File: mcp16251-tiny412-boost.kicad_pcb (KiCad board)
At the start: 2 copper layers, 40.6 x 24.1 mm, 40 parts, among them J1 JST_PH_Header, J10 THT_Castellated, J11 THT_Castellated, J2 THT_Castellated, J3 THT_Castellated, J4 THT_Castellated, J5 THT_Castellated, J6 THT_Castellated, J7 THT_Castellated, J8 THT_Castellated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

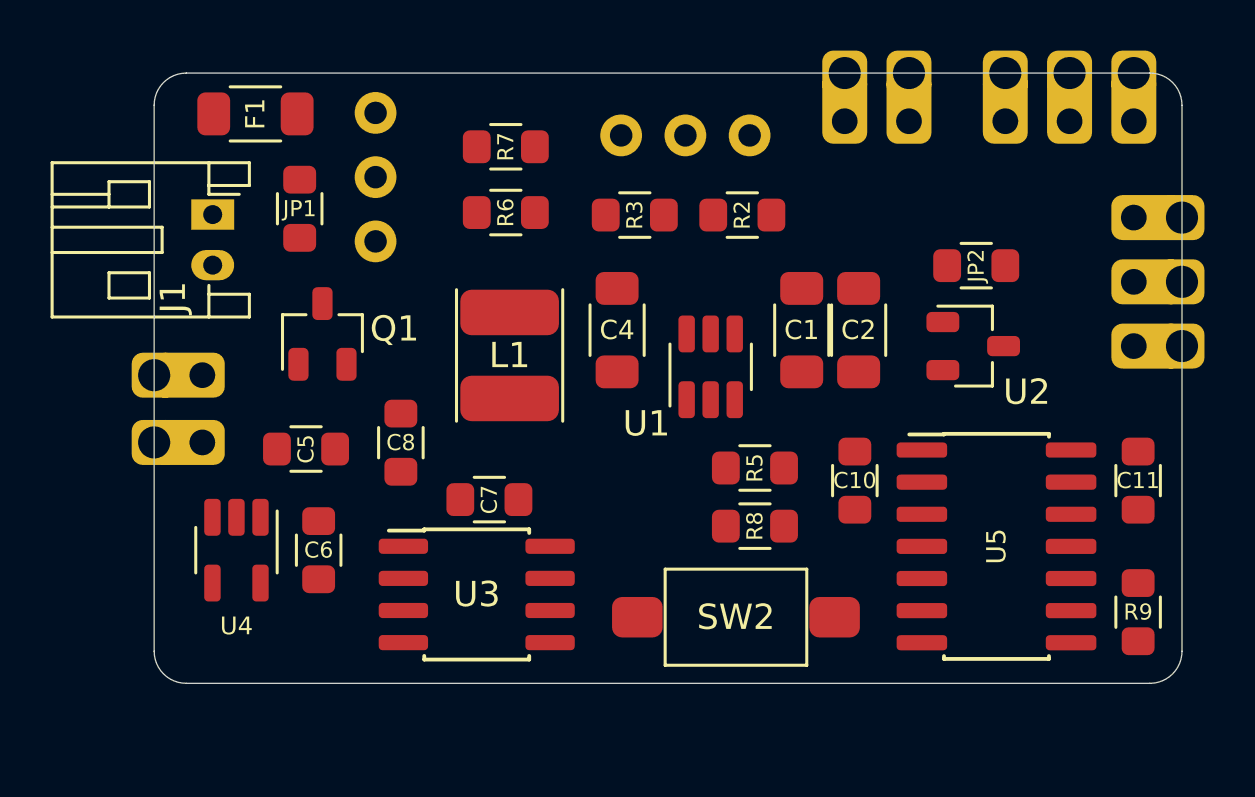
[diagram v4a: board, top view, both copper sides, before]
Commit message: Step-up converter sub-circuit wiring
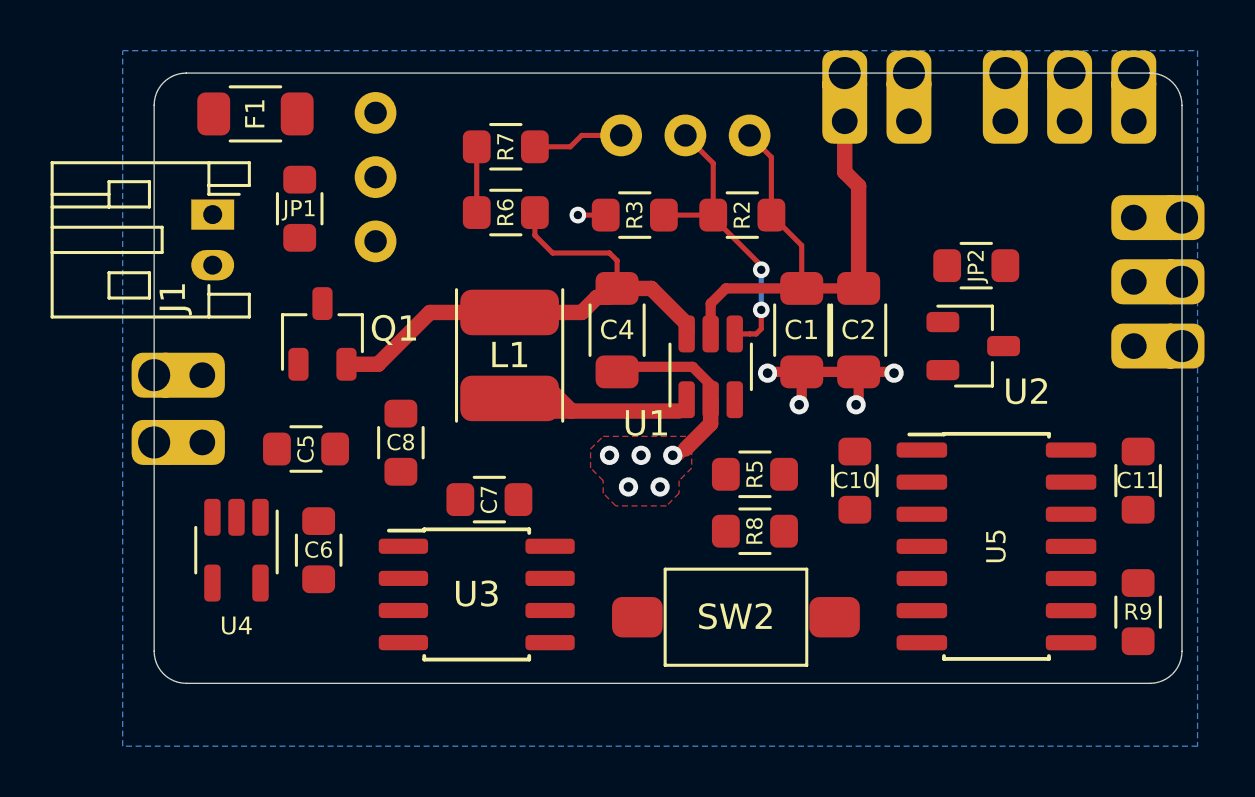
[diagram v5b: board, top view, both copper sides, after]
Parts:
- moved R5 0.25 mm to (142.5, 111.8)
- moved R8 0.20 mm to (142.5, 114.0)
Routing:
- net VBAT: track 0.00 -> 21.3 mm
- net 5V: track 0.00 -> 21.0 mm
- net GND: track 0.00 -> 20.1 mm, vias 0 -> 10
- net Net-(R2-Pad2): track 0.00 -> 12.0 mm, vias 0 -> 2
- net Net-(L1-Pad2): track 0.00 -> 6.56 mm
- net Net-(C8-Pad2): track 0.00 -> 2.60 mm
- added copper zone on B.Cu, net GND
- added copper zone on F.Cu, net GND
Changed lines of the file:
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@@
     (thickness 1.6)
     (drawings 12)
-    (tracks 0)
+    (tracks 74)
     (zones 0)
     (modules 40)
@@
   )
   (module MCP16251_module:0805_HS (layer F.Cu)
-    (at 142.5 111.5 180)
+    (at 142.5 111.75 180)
     (descr "Resistor SMD 0805, reflow soldering, Vishay (see dcrcw.pdf)")
     (tags "resistor 0805")
@@
   )
   (module MCP16251_module:0805_HS (layer F.Cu)
-    (at 142.5 113.8 180)
+    (at 142.5 114 180)
     (descr "Resistor SMD 0805, reflow soldering, Vishay (see dcrcw.pdf)")
     (tags "resistor 0805")
@@
     (arrow2b (pts (xy 118.745 129.54) (xy 119.871504 128.953579)))
   )
+  (via (at 138 111) (size 0.762) (drill 0.381) (layers F.Cu B.Cu) (net 1))
+  (segment (start 134.5 108.5) (end 135.25 109.25) (width 0.6096) (layer F.Cu) (net 4))
+  (segment (start 134 109.25) (end 139.5 109.25) (width 0.6096) (layer F.Cu) (net 4))
+  (segment (start 137.25 107.5) (end 137.05 107.7) (width 0.4064) (layer F.Cu) (net 1))
+  (segment (start 140.034562 107.5) (end 137.25 107.5) (width 0.4064) (layer F.Cu) (net 1))
+  (segment (start 140.75 108.215438) (end 140.034562 107.5) (width 0.4064) (layer F.Cu) (net 1))
+  (segment (start 140.75 108.8) (end 140.75 108.215438) (width 0.4064) (layer F.Cu) (net 1))
+  (segment (start 144.35 107.7) (end 146.6 107.7) (width 0.4064) (layer F.Cu) (net 1))
+  (via (at 139.25 111) (size 0.762) (drill 0.381) (layers F.Cu B.Cu) (net 1))
+  (segment (start 139.5 111) (end 139.25 111) (width 0.4064) (layer F.Cu) (net 1))
+  (via (at 136.75 111) (size 0.762) (drill 0.381) (layers F.Cu B.Cu) (net 1))
+  (via (at 138.75 112.25) (size 0.762) (drill 0.381) (layers F.Cu B.Cu) (net 1))
+  (via (at 137.5 112.25) (size 0.762) (drill 0.381) (layers F.Cu B.Cu) (net 1))
+  (segment (start 140.75 108.8) (end 140.75 109.75) (width 0.6096) (layer F.Cu) (net 1))
+  (segment (start 140.75 109.75) (end 139.75 110.75) (width 0.6096) (layer F.Cu) (net 1))
+  (segment (start 139.75 110.75) (end 139.5 111) (width 0.4064) (layer F.Cu) (net 1))
+  (segment (start 144.35 108.9) (end 144.25 109) (width 0.4064) (layer F.Cu) (net 1))
+  (via (at 144.25 109) (size 0.762) (drill 0.381) (layers F.Cu B.Cu) (net 1))
+  (segment (start 144.35 107.7) (end 144.35 108.9) (width 0.4064) (layer F.Cu) (net 1))
+  (via (at 146.5 109) (size 0.762) (drill 0.381) (layers F.Cu B.Cu) (net 1))
+  (segment (start 146.6 108.9) (end 146.5 109) (width 0.4064) (layer F.Cu) (net 1))
+  (segment (start 146.6 107.7) (end 146.6 108.9) (width 0.4064) (layer F.Cu) (net 1))
+  (via (at 148 107.75) (size 0.762) (drill 0.381) (layers F.Cu B.Cu) (net 1))
+  (segment (start 147.95 107.7) (end 148 107.75) (width 0.4064) (layer F.Cu) (net 1))
+  (segment (start 146.6 107.7) (end 147.95 107.7) (width 0.4064) (layer F.Cu) (net 1))
+  (via (at 143 107.75) (size 0.762) (drill 0.381) (layers F.Cu B.Cu) (net 1))
+  (segment (start 143.05 107.7) (end 143 107.75) (width 0.4064) (layer F.Cu) (net 1))
+  (segment (start 144.35 107.7) (end 143.05 107.7) (width 0.4064) (layer F.Cu) (net 1))
+  (segment (start 137.15 98.35) (end 137.21 98.35) (width 0.2032) (layer F.Cu) (net 1))
+  (segment (start 133.8 98.8) (end 135.2 98.8) (width 0.2032) (layer F.Cu) (net 1))
+  (segment (start 135.65 98.35) (end 137.21 98.35) (width 0.2032) (layer F.Cu) (net 1))
+  (segment (start 135.2 98.8) (end 135.65 98.35) (width 0.2032) (layer F.Cu) (net 1))
+  (via (at 135.5 101.5) (size 0.6604) (drill 0.3302) (layers F.Cu B.Cu) (net 1))
+  (segment (start 136.6 101.5) (end 135.5 101.5) (width 0.2032) (layer F.Cu) (net 1))
+  (segment (start 126.35 107.4) (end 127.6 107.4) (width 0.6096) (layer F.Cu) (net 2))
+  (segment (start 129.65 105.35) (end 132.8 105.35) (width 0.6096) (layer F.Cu) (net 2))
+  (segment (start 127.6 107.4) (end 129.65 105.35) (width 0.6096) (layer F.Cu) (net 2))
+  (segment (start 139.8 105.8) (end 139.8 106.2) (width 0.6096) (layer F.Cu) (net 2))
+  (segment (start 138.4 104.4) (end 139.8 105.8) (width 0.6096) (layer F.Cu) (net 2))
+  (segment (start 137.05 104.4) (end 138.4 104.4) (width 0.6096) (layer F.Cu) (net 2))
+  (segment (start 135.65 105.35) (end 136.25 104.75) (width 0.6096) (layer F.Cu) (net 2))
+  (segment (start 136.7 104.75) (end 137.05 104.4) (width 0.6096) (layer F.Cu) (net 2))
+  (segment (start 136.25 104.75) (end 136.7 104.75) (width 0.6096) (layer F.Cu) (net 2))
+  (segment (start 132.8 105.35) (end 135.65 105.35) (width 0.6096) (layer F.Cu) (net 2))
+  (segment (start 133.8 102.3) (end 133.8 101.4) (width 0.2032) (layer F.Cu) (net 2))
+  (segment (start 136.75 103) (end 134.5 103) (width 0.2032) (layer F.Cu) (net 2))
+  (segment (start 134.5 103) (end 133.8 102.3) (width 0.2032) (layer F.Cu) (net 2))
+  (segment (start 137.05 103.3) (end 136.75 103) (width 0.2032) (layer F.Cu) (net 2))
+  (segment (start 137.05 104.4) (end 137.05 103.3) (width 0.2032) (layer F.Cu) (net 2))
+  (segment (start 141.7 106.2) (end 142.3 106.2) (width 0.2032) (layer F.Cu) (net 5))
+  (segment (start 142.3 106.2) (end 142.55 106.2) (width 0.2032) (layer F.Cu) (net 5))
+  (segment (start 142.75 106) (end 142.75 105.25) (width 0.2032) (layer F.Cu) (net 5))
+  (via (at 142.75 105.25) (size 0.6604) (drill 0.3302) (layers F.Cu B.Cu) (net 5))
+  (segment (start 142.55 106.2) (end 142.75 106) (width 0.2032) (layer F.Cu) (net 5))
+  (via (at 142.75 103.6634) (size 0.6604) (drill 0.3302) (layers F.Cu B.Cu) (net 5))
+  (segment (start 142.75 105.25) (end 142.75 103.6634) (width 0.2032) (layer B.Cu) (net 5))
+  (segment (start 142.75 103.6634) (end 142.75 103.5) (width 0.2032) (layer F.Cu) (net 5))
+  (segment (start 140.85 101.6) (end 140.85 101.5) (width 0.2032) (layer F.Cu) (net 5))
+  (segment (start 142.75 103.5) (end 140.85 101.6) (width 0.2032) (layer F.Cu) (net 5))
+  (segment (start 140.85 101.5) (end 138.9 101.5) (width 0.2032) (layer F.Cu) (net 5))
+  (segment (start 140.85 99.45) (end 139.75 98.35) (width 0.2032) (layer F.Cu) (net 5))
+  (segment (start 140.85 101.5) (end 140.85 99.45) (width 0.2032) (layer F.Cu) (net 5))
+  (segment (start 141.35 104.4) (end 144.35 104.4) (width 0.4064) (layer F.Cu) (net 6))
+  (segment (start 140.75 105) (end 141.35 104.4) (width 0.4064) (layer F.Cu) (net 6))
+  (segment (start 140.75 106.2) (end 140.75 105) (width 0.4064) (layer F.Cu) (net 6))
+  (segment (start 144.35 104.4) (end 146.6 104.4) (width 0.4064) (layer F.Cu) (net 6))
+  (segment (start 146.6 104.4) (end 146.6 100.35) (width 0.6096) (layer F.Cu) (net 6))
+  (segment (start 146.05 99.8) (end 146.05 97.79) (width 0.6096) (layer F.Cu) (net 6))
+  (segment (start 146.6 100.35) (end 146.05 99.8) (width 0.6096) (layer F.Cu) (net 6))
+  (segment (start 144.35 102.7) (end 143.15 101.5) (width 0.2032) (layer F.Cu) (net 6))
+  (segment (start 144.35 104.4) (end 144.35 102.7) (width 0.2032) (layer F.Cu) (net 6))
+  (segment (start 143.15 99.21) (end 142.29 98.35) (width 0.2032) (layer F.Cu) (net 6))
+  (segment (start 143.15 101.5) (end 143.15 99.21) (width 0.2032) (layer F.Cu) (net 6))
+  (segment (start 131.5 98.8) (end 131.5 101.4) (width 0.2032) (layer F.Cu) (net 10))
+  (zone (net 1) (net_name GND) (layer F.Cu) (hatch edge 0.508)
+    (connect_pads (clearance 0.4064))
+    (min_thickness 0.254)
+    (fill yes (arc_segments 32) (thermal_gap 0.508) (thermal_bridge_width 0.508) (smoothing fillet) (radius 1))
+    (polygon
+      (pts
+        (xy 136 110.75) (xy 136.5 110.25) (xy 140.25 110.25) (xy 140 110.75) (xy 140 111.5)
+        (xy 139.5 112) (xy 139.5 112.5) (xy 139 113) (xy 137 113) (xy 136.5 112.5)
+        (xy 136.5 112) (xy 136 111.5)
+      )
+    )
+  )
+  (zone (net 1) (net_name GND) (layer B.Cu) (hatch edge 0.508)
+    (connect_pads (clearance 0.4064))
+    (min_thickness 0.254)
+    (fill yes (arc_segments 32) (thermal_gap 0.508) (thermal_bridge_width 0.508) (smoothing fillet) (radius 1))
+    (polygon
+      (pts
+        (xy 117.5 95) (xy 160 95) (xy 160 122.5) (xy 117.5 122.5)
+      )
+    )
+  )
 )

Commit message: Complete routing, pending verification
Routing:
- net GND: track 20.1 -> 78.2 mm, vias 10 -> 25
- net 2V5: track 0.00 -> 33.9 mm
- net TXD: track 0.00 -> 22.8 mm
- net BOOST_EN: track 0.00 -> 21.4 mm, vias 0 -> 2
- net Net-(C8-Pad2): track 2.60 -> 21.1 mm, vias 0 -> 4
- net TXD_HV: track 0.00 -> 18.4 mm, vias 0 -> 1
- net UPDI_HV: track 0.00 -> 18.2 mm, vias 0 -> 2
- net VIN_HV: track 0.00 -> 18.0 mm
- net RXD_HV: track 0.00 -> 17.9 mm, vias 0 -> 1
- net RXD: track 0.00 -> 16.4 mm
- net SHIFT_EN: track 0.00 -> 16.3 mm
- net VBAT: track 21.3 -> 34.9 mm, vias 0 -> 2
- net VBAT_RAW: track 0.00 -> 12.5 mm
- net Net-(R8-Pad2): track 0.00 -> 9.55 mm
- net UPDI: track 0.00 -> 6.63 mm
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
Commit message: Check layout, add silkscreen
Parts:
- added REF***: OSHW-Logo_5.7x6mm_SilkScreen, Symbols:OSHW-Logo_5.7x6mm_SilkScreen, B.Cu at (132.2, 100.2)
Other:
- board text added: "(C) Vlad Belous CC BY-SA 4.0"
- board text added: "5V"
- board text added: "AP7354"
- board text added: "G"
- board text added: "GND"
- board text added: "MCP16251 step-up with ATTINY412"
- board text added: "NOTES:"
- board text added: "OFF"
- board text added: "ON"
- board text added: "PA0"
- board text added: "RHI"
- board text added: "RLO"
- board text added: "RXD"
- board text added: "TXB0104"
- board text added: "TXD"
- board text added: "UPDI"
- board text added: "V+"
- board text added: "VBAT"
- board text added: "VHI"
- board text added: "t412"
